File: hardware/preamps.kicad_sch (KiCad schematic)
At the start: 29 parts, among them J1 AudioJack2, J2 AudioJack2, J3 Conn_02x05_Odd_Even, U1 TL072, U2 TL072

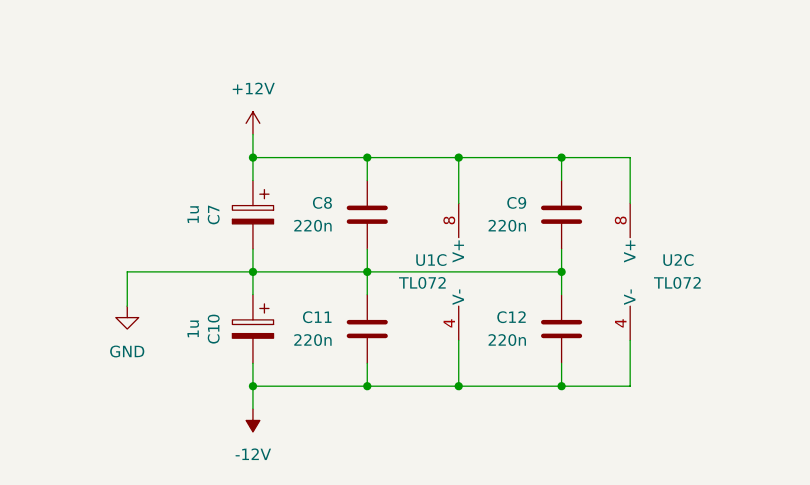
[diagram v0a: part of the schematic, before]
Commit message: analog conditioning and preamp board sent for prototype manufacture
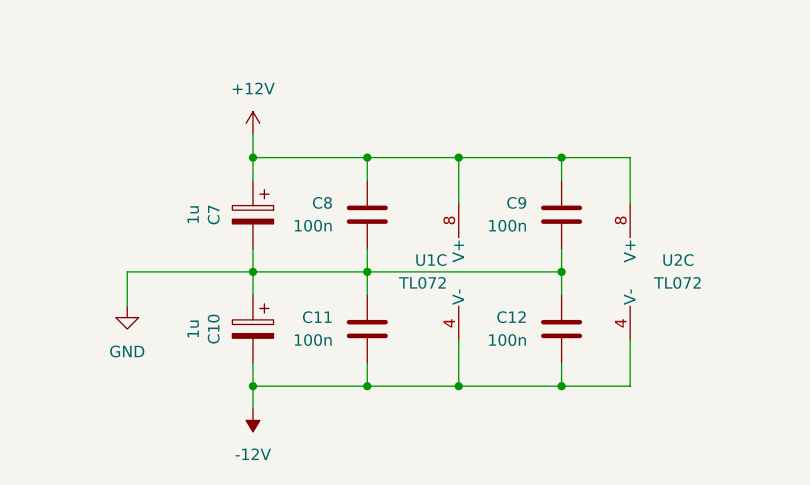
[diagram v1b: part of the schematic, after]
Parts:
- C11, C12, C8, C9: value 220n -> 100n
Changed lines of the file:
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@@
 			)
 		)
-		(property "Value" "220n"
+		(property "Value" "100n"
 			(at 63.5 144.7799 0)
 			(effects
@@
 			)
 		)
-		(property "Value" "220n"
+		(property "Value" "100n"
 			(at 85.09 144.7799 0)
 			(effects
@@
 			)
 		)
-		(property "Value" "220n"
+		(property "Value" "100n"
 			(at 85.09 132.0799 0)
 			(effects
@@
 			)
 		)
-		(property "Value" "220n"
+		(property "Value" "100n"
 			(at 63.5 132.0799 0)
 			(effects
